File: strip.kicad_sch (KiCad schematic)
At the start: 44 parts, among them J102 WAGO-2065, J103 WAGO-2065, J104 WAGO-2065, J105 CORTEX-DEBUG, J106 JAE DX07S016JA1R1500, SW101 SW_Push, SW102 SW_Push, U101 74AHC1G125, U102 ATSAMD51G, U103 AP2112K-3.3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

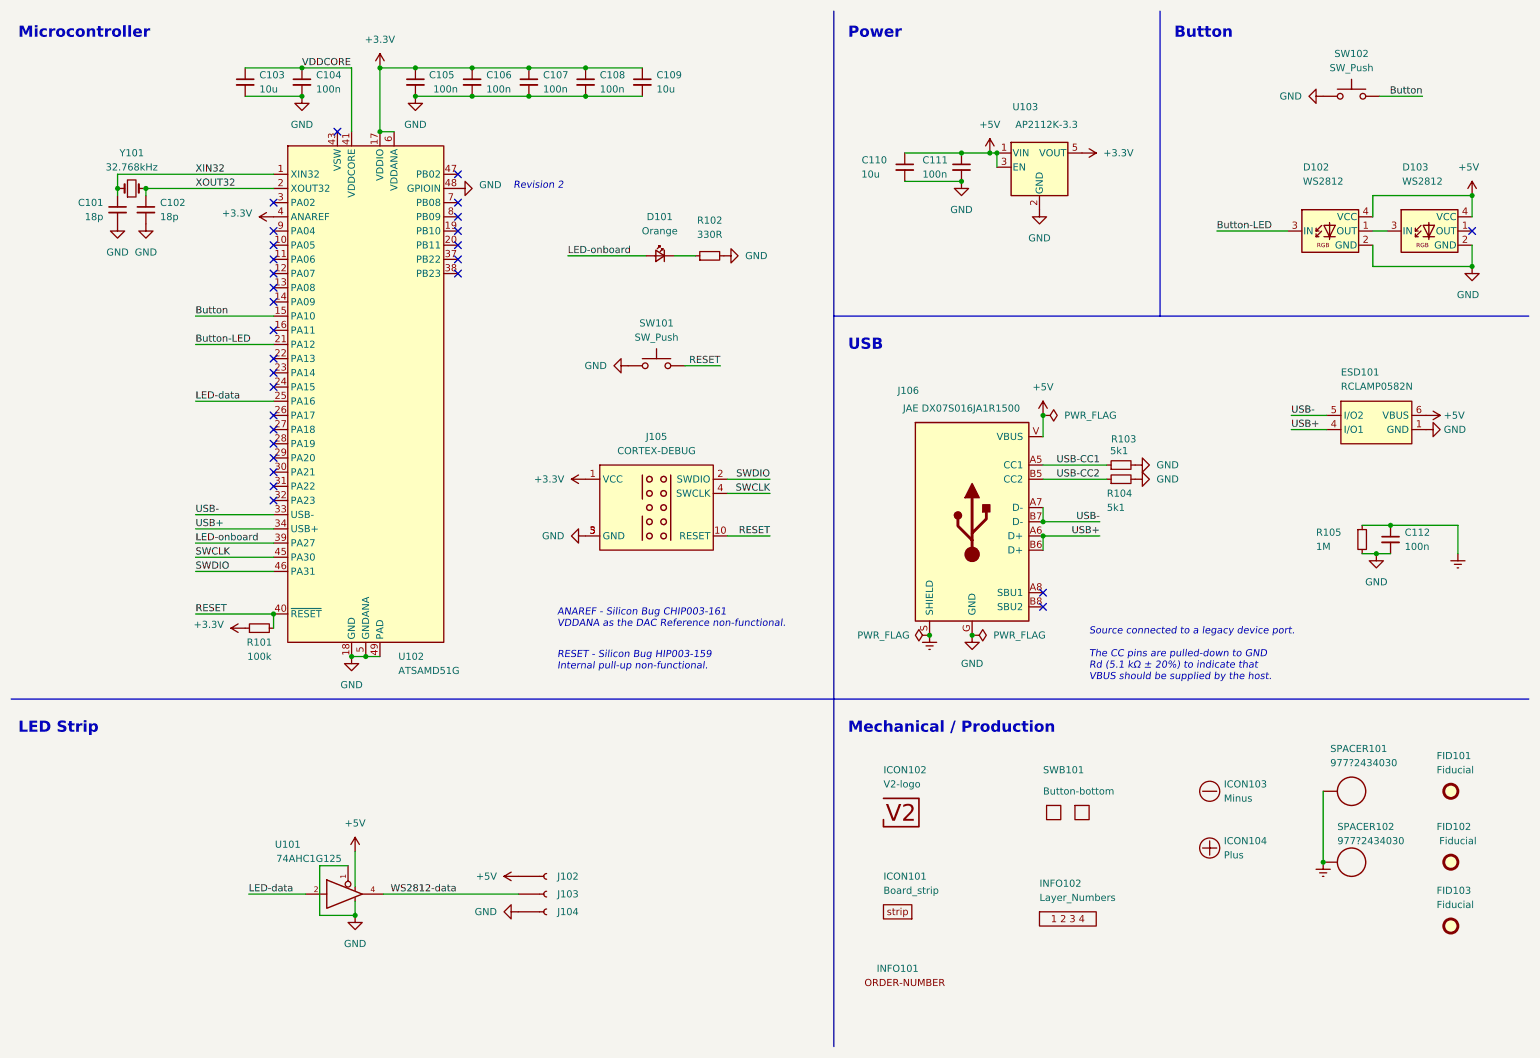
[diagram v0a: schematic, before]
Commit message: Update to KiCad 7.0
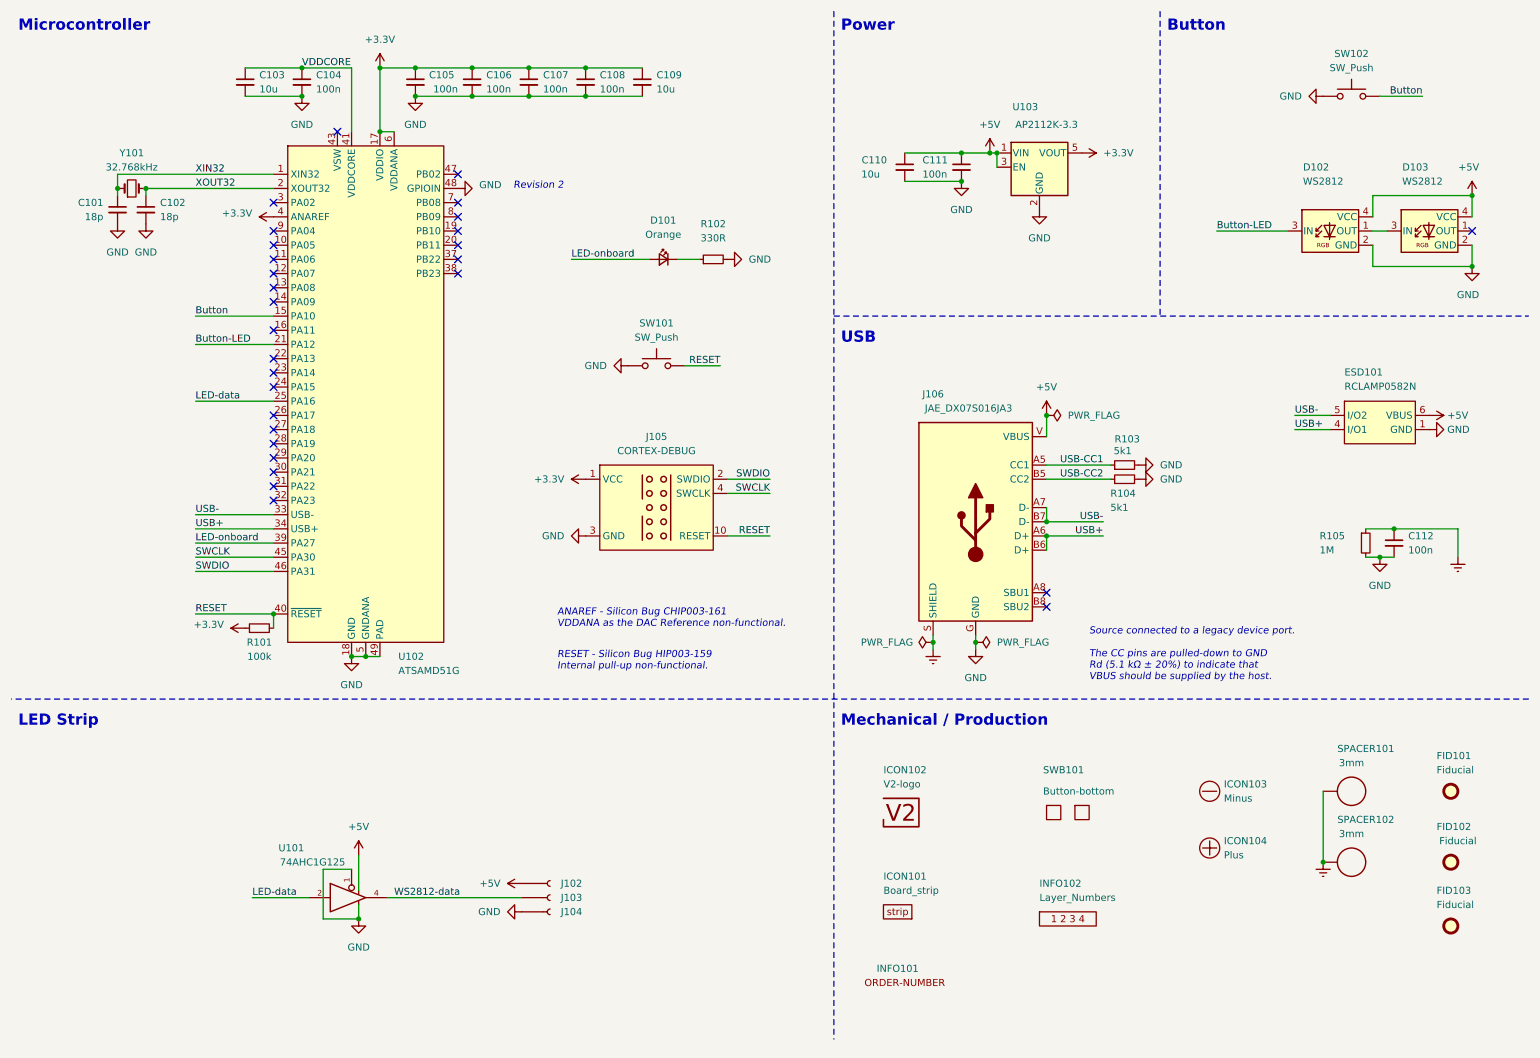
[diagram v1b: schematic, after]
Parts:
- J106: value JAE DX07S016JA1R1500 -> JAE_DX07S016JA3; footprint V2_Connector_USB:JAE_DX07S016JA1R1500 -> V2_Connector_USB:JAE_DX07S016JA3; symbol V2_Connector_USB:JAE_DX07S016JA1R1500 -> V2_Connector_USB:JAE_DX07S016JA3
- SPACER101, SPACER102: value 977?2434030 -> 3mm; symbol V2_Spacer_Wurth:977?2434030 -> V2_Spacer_Wurth:9774030243
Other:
- moved on the sheet: C112, D101, ESD101, J102, J103, J104, J106, R102, R103, R104, R105, U101
